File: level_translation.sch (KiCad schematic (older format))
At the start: 4 parts, among them U17 TXB0104PW, U18 TXB0104PW

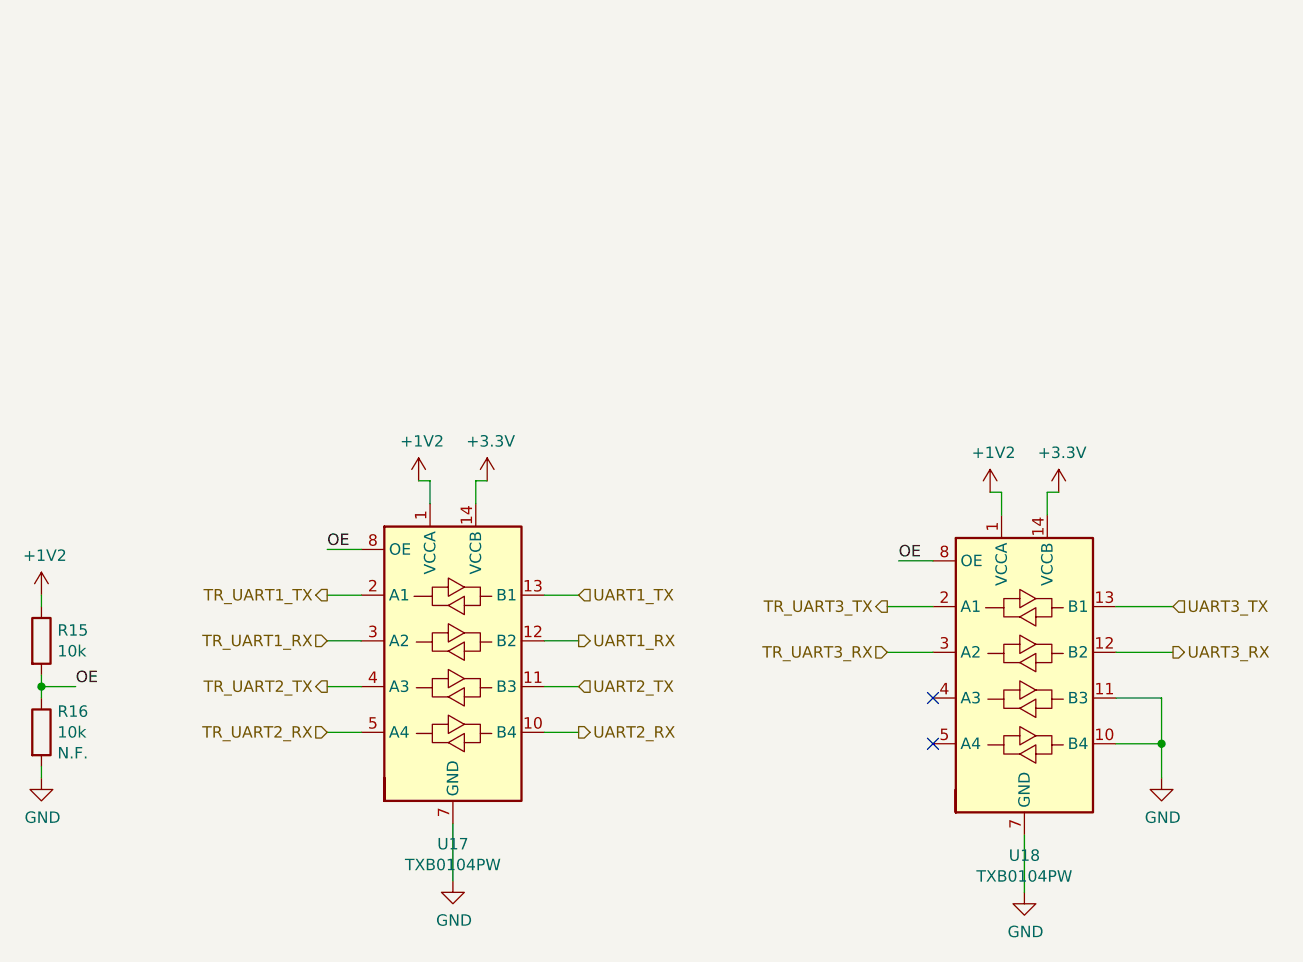
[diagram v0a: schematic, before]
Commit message: Supply caps, initial signal states and headers
  * Added bulk supply caps.
  * Set initial control signal states via resistors.
  * Add debug headers.
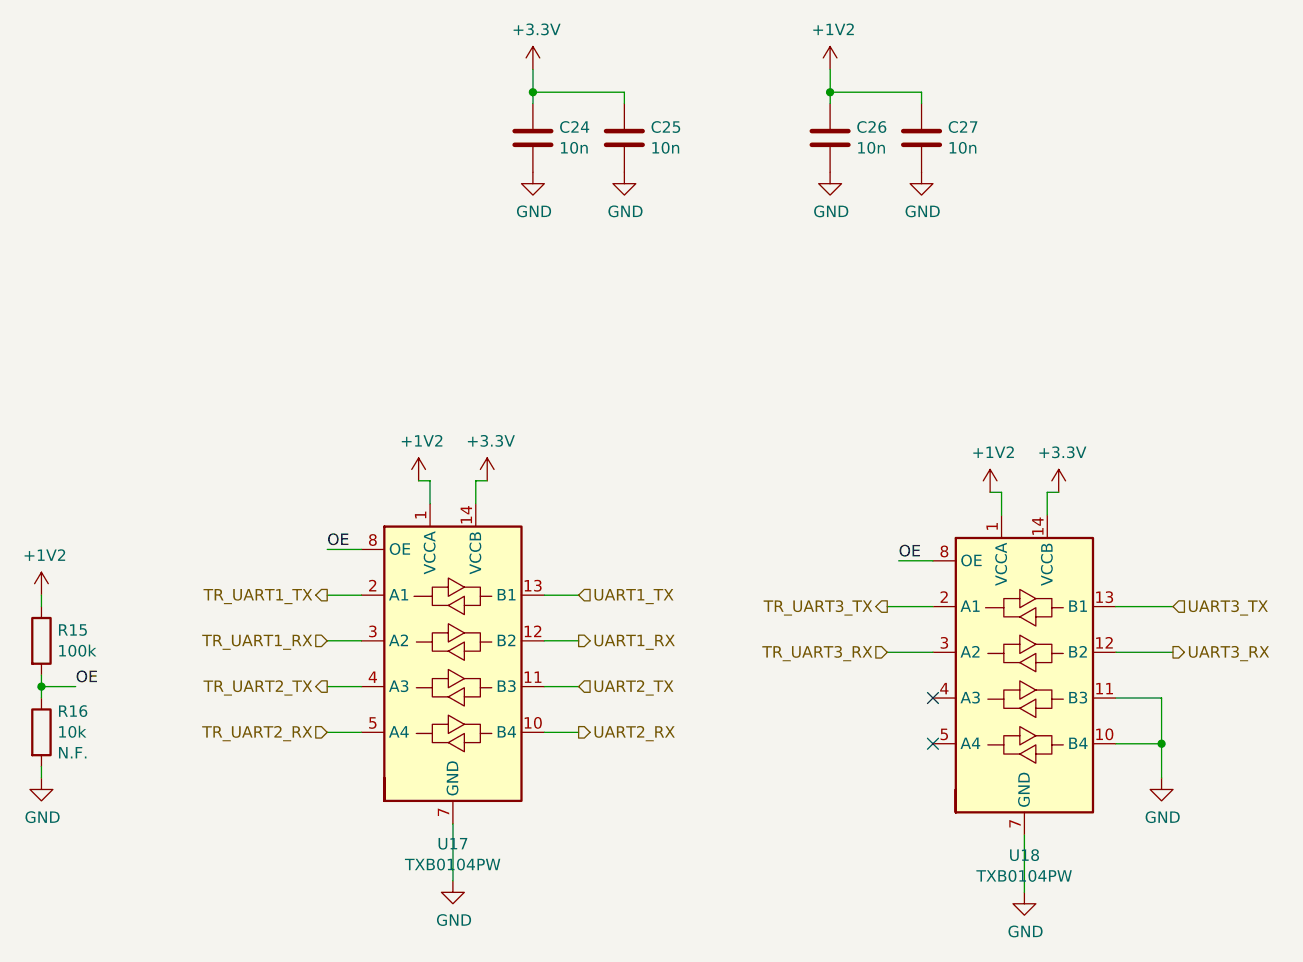
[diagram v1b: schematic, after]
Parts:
- added C24, C25, C26, C27: 10n, symbol Device:C
- R15: value 10k -> 100k
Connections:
- net +1V2: now also C26.1, C27.1
- net +3V3: now also C24.1, C25.1
- net GND: now also C24.2, C25.2, C26.2, C27.2
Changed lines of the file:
@@
 AR Path="/61BE2A8A/619F3501/619F4E70" Ref="R15"  Part="1"
 F 0 "R15" H 2820 3946 50  0000 L CNN
-F 1 "10k" H 2820 3855 50  0000 L CNN
+F 1 "100k" H 2820 3855 50  0000 L CNN
 F 2 "" V 2680 3900 50  0001 C CNN
 F 3 "~" H 2750 3900 50  0001 C CNN
@@
 NoConn ~ 6650 4150
 NoConn ~ 6650 4350
+$Comp
+L Device:C C24
+U 1 1 61B738B0
+P 4900 1700
+F 0 "C24" H 5015 1746 50  0000 L CNN
+F 1 "10n" H 5015 1655 50  0000 L CNN
+F 2 "" H 4938 1550 50  0001 C CNN
+F 3 "~" H 4900 1700 50  0001 C CNN
+	1    4900 1700
+	1    0    0    -1
+$EndComp
+$Comp
+L power:GND #PWR0146
+U 1 1 61B738B6
+P 4900 1850
+F 0 "#PWR0146" H 4900 1600 50  0001 C CNN
+F 1 "GND" H 4905 1677 50  0000 C CNN
+F 2 "" H 4900 1850 50  0001 C CNN
+F 3 "" H 4900 1850 50  0001 C CNN
+	1    4900 1850
+	1    0    0    -1
+$EndComp
+$Comp
+L power:+3.3V #PWR0147
+U 1 1 61B738BC
+P 4900 1400
+F 0 "#PWR0147" H 4900 1250 50  0001 C CNN
+F 1 "+3.3V" H 4915 1573 50  0000 C CNN
+F 2 "" H 4900 1400 50  0001 C CNN
+F 3 "" H 4900 1400 50  0001 C CNN
+	1    4900 1400
+	1    0    0    -1
+$EndComp
+$Comp
+L Device:C C25
+U 1 1 61B738C2
+P 5300 1700
+F 0 "C25" H 5415 1746 50  0000 L CNN
+F 1 "10n" H 5415 1655 50  0000 L CNN
+F 2 "" H 5338 1550 50  0001 C CNN
+F 3 "~" H 5300 1700 50  0001 C CNN
+	1    5300 1700
+	1    0    0    -1
+$EndComp
+$Comp
+L power:GND #PWR0148
+U 1 1 61B738C8
+P 5300 1850
+F 0 "#PWR0148" H 5300 1600 50  0001 C CNN
+F 1 "GND" H 5305 1677 50  0000 C CNN
+F 2 "" H 5300 1850 50  0001 C CNN
+F 3 "" H 5300 1850 50  0001 C CNN
+	1    5300 1850
+	1    0    0    -1
+$EndComp
+Wire Wire Line
+	4900 1500 4900 1400
+Wire Wire Line
+	4900 1500 4900 1550
+Connection ~ 4900 1500
+Wire Wire Line
+	5300 1500 5300 1550
+Wire Wire Line
+	5300 1500 4900 1500
+$Comp
+L Device:C C26
+U 1 1 61B768DC
+P 6200 1700
+F 0 "C26" H 6315 1746 50  0000 L CNN
+F 1 "10n" H 6315 1655 50  0000 L CNN
+F 2 "" H 6238 1550 50  0001 C CNN
+F 3 "~" H 6200 1700 50  0001 C CNN
+	1    6200 1700
+	1    0    0    -1
+$EndComp
+$Comp
+L power:GND #PWR0149
+U 1 1 61B768E2
+P 6200 1850
+F 0 "#PWR0149" H 6200 1600 50  0001 C CNN
+F 1 "GND" H 6205 1677 50  0000 C CNN
+F 2 "" H 6200 1850 50  0001 C CNN
+F 3 "" H 6200 1850 50  0001 C CNN
+	1    6200 1850
+	1    0    0    -1
+$EndComp
+$Comp
+L Device:C C27
+U 1 1 61B768EE
+P 6600 1700
+F 0 "C27" H 6715 1746 50  0000 L CNN
+F 1 "10n" H 6715 1655 50  0000 L CNN
+F 2 "" H 6638 1550 50  0001 C CNN
+F 3 "~" H 6600 1700 50  0001 C CNN
+	1    6600 1700
+	1    0    0    -1
+$EndComp
+$Comp
+L power:GND #PWR0150
+U 1 1 61B768F4
+P 6600 1850
+F 0 "#PWR0150" H 6600 1600 50  0001 C CNN
+F 1 "GND" H 6605 1677 50  0000 C CNN
+F 2 "" H 6600 1850 50  0001 C CNN
+F 3 "" H 6600 1850 50  0001 C CNN
+	1    6600 1850
+	1    0    0    -1
+$EndComp
+Wire Wire Line
+	6200 1500 6200 1400
+Wire Wire Line
+	6200 1500 6200 1550
+Connection ~ 6200 1500
+Wire Wire Line
+	6600 1500 6600 1550
+Wire Wire Line
+	6600 1500 6200 1500
+$Comp
+L power:+1V2 #PWR0151
+U 1 1 61B78006
+P 6200 1400
+F 0 "#PWR0151" H 6200 1250 50  0001 C CNN
+F 1 "+1V2" H 6215 1573 50  0000 C CNN
+F 2 "" H 6200 1400 50  0001 C CNN
+F 3 "" H 6200 1400 50  0001 C CNN
+	1    6200 1400
+	1    0    0    -1
+$EndComp
 $EndSCHEMATC

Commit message: Replace MCU by something available in distributors
Given the current chip shortage the STM32F0 was not available from
JLCPCB. This one (STM32F411CE) is available in large quantities from
JLCPCB. Despite being much more powerful than the F0, it is still in the
price range and actually cheaper than the STM32F103C8T6... which I don't
understand...
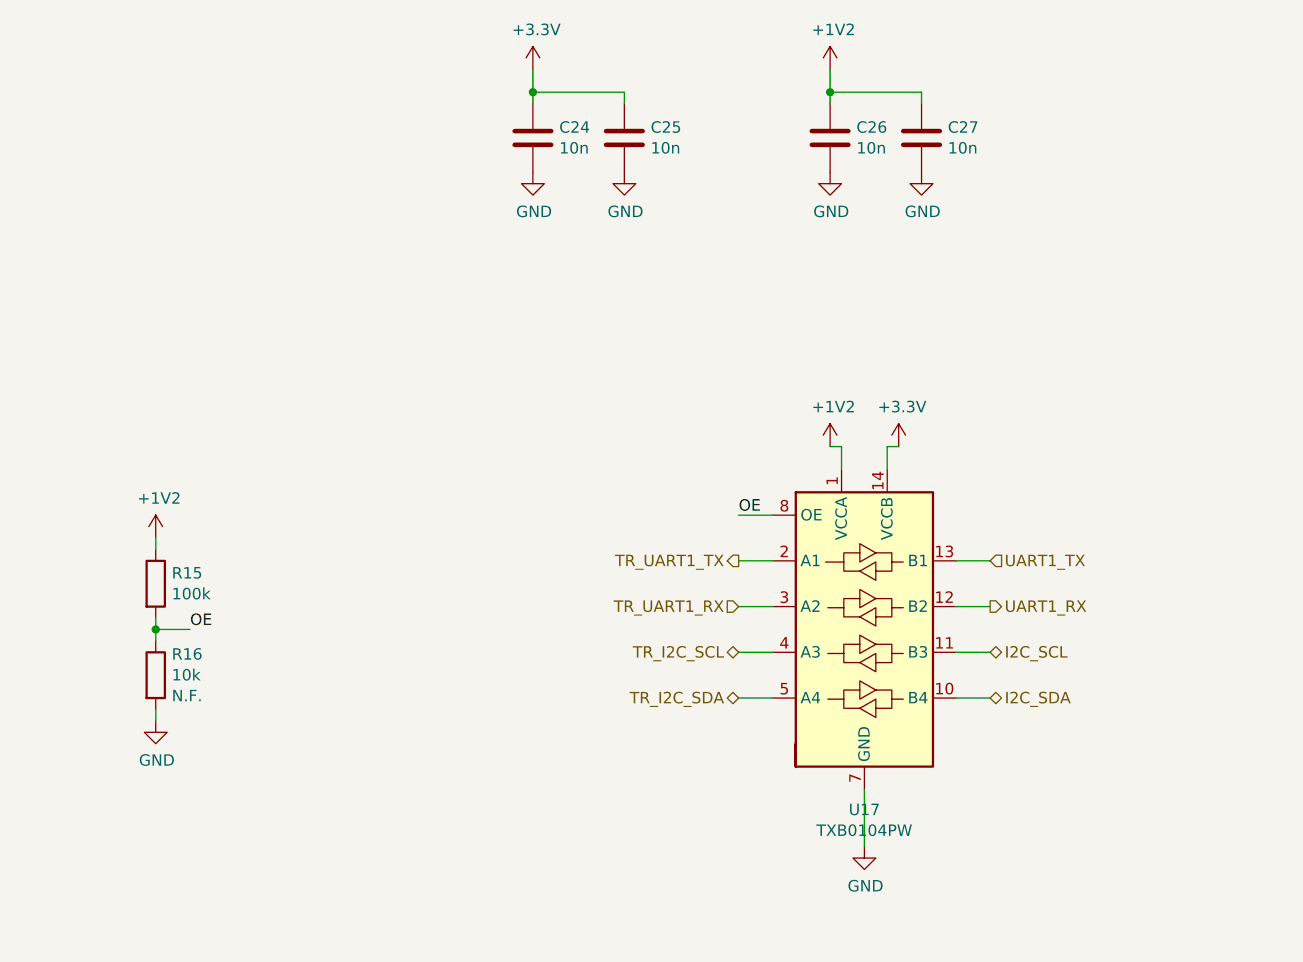
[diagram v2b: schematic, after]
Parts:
- removed U18: TXB0104PW, Package_SO:TSSOP-14_4.4x5mm_P0.65mm, symbol Logic_LevelTranslator:TXB0104PW
- U17: LCSC (none) -> C60708
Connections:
- net TR_UART2_RX renamed TR_I2C_SDA
- net TR_UART2_TX renamed TR_I2C_SCL
- net UART2_RX renamed I2C_SDA
- net UART2_TX renamed I2C_SCL
- no-connect marks 2 -> 0
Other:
- moved on the sheet: R15, R16, U17
